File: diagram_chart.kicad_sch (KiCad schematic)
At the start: 3 parts

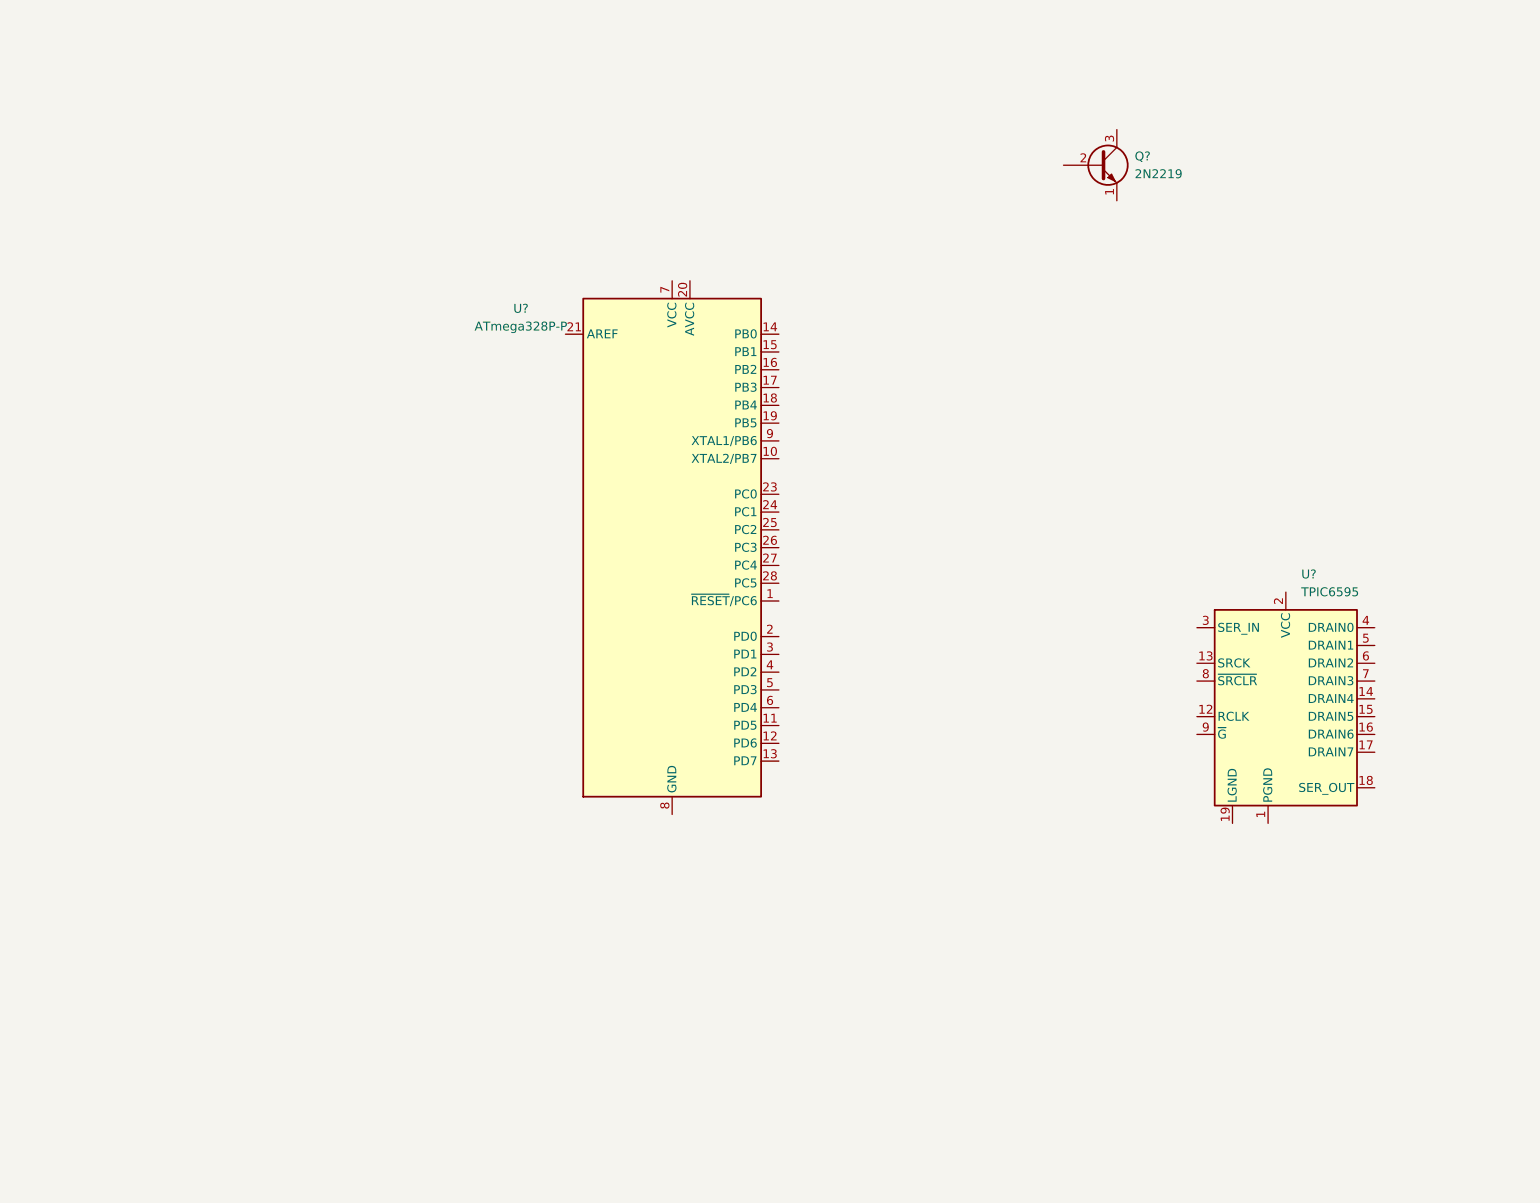
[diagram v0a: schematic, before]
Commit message: Added custom footprint and need to look at show to include it
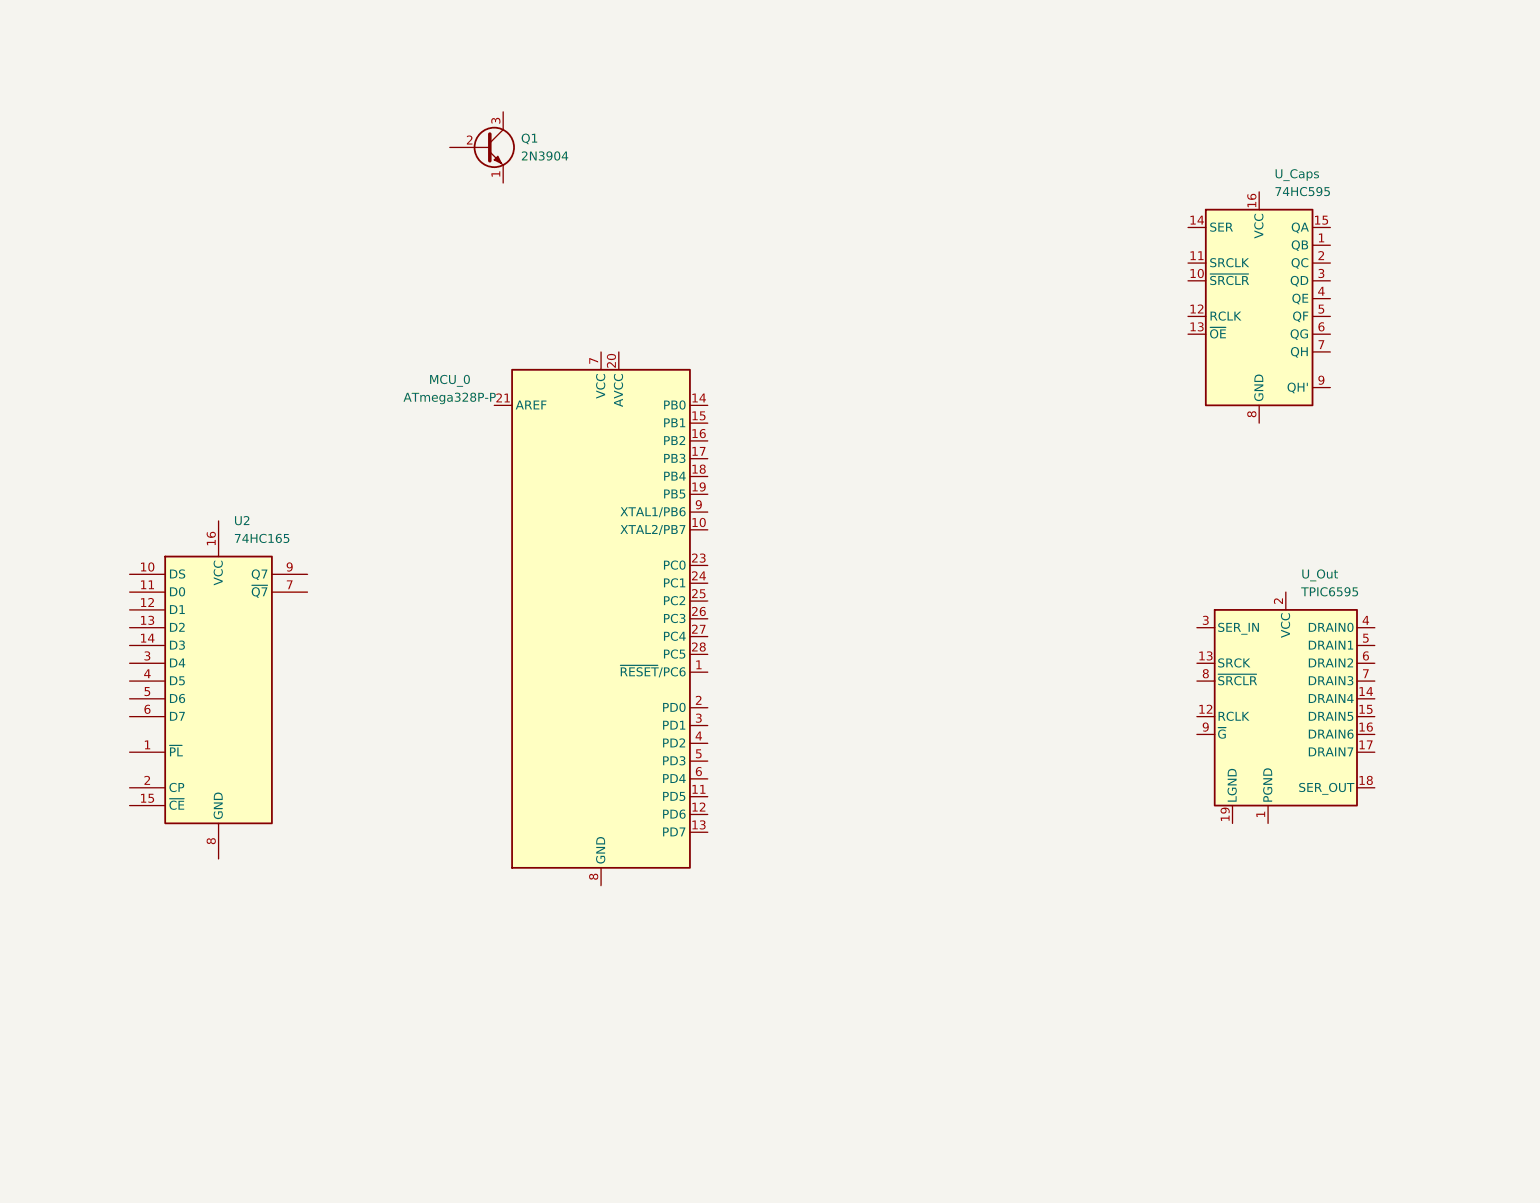
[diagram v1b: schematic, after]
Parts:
- removed Q?: 2N2219, Package_TO_SOT_THT:TO-39-3, symbol Transistor_BJT:2N2219
- added Q1: 2N3904, Package_TO_SOT_THT:TO-92_Inline, symbol Transistor_BJT:2N3904
- added U2: 74HC165, Package_DIP:DIP-16_W7.62mm_Socket, symbol 74xx:74HC165
- added U_Caps: 74HC595, Package_DIP:DIP-16_W7.62mm_Socket, symbol 74xx:74HC595
- MCU_0: renamed from U?; footprint Package_DIP:DIP-28_W7.62mm -> Package_DIP:DIP-28_W7.62mm_Socket
- U_Out: renamed from U?; footprint Package_DIP:DIP-20_W7.62mm -> Package_DIP:DIP-16_W7.62mm_Socket
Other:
- moved on the sheet: MCU_0
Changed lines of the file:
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@@
 (kicad_sch (version 20230121) (generator eeschema)
   (paper "A4")
-  (symbol (lib_id "Transistor_BJT:2N2219") (at 196.85 40.64 0) (unit 1)
+  (symbol (lib_id "74xx:74HC165") (at 71.12 114.3 0) (unit 1)
     (in_bom yes) (on_board yes) (dnp no) (fields_autoplaced)
-    (property "Reference" "Q?" (at 201.93 39.37 0)
+    (property "Reference" "U2" (at 73.3141 91.44 0)
       (effects (font (size 1.27 1.27)) (justify left))
     )
-    (property "Value" "2N2219" (at 201.93 41.91 0)
+    (property "Value" "74HC165" (at 73.3141 93.98 0)
       (effects (font (size 1.27 1.27)) (justify left))
     )
-    (property "Footprint" "Package_TO_SOT_THT:TO-39-3" (at 201.93 42.545 0)
-      (effects (font (size 1.27 1.27) italic) (justify left) hide)
+    (property "Footprint" "Package_DIP:DIP-16_W7.62mm_Socket" (at 71.12 114.3 0)
+      (effects (font (size 1.27 1.27)) hide)
     )
-    (property "Datasheet" "http://www.onsemi.com/pub_link/Collateral/2N2219-D.PDF" (at 196.85 40.64 0)
-      (effects (font (size 1.27 1.27)) (justify left) hide)
+    (property "Datasheet" "https://assets.nexperia.com/documents/data-sheet/74HC_HCT165.pdf" (at 71.12 114.3 0)
+      (effects (font (size 1.27 1.27)) hide)
     )
+    (pin "7")
+    (pin "12")
     (pin "2")
+    (pin "15")
+    (pin "13")
+    (pin "16")
+    (pin "8")
+    (pin "6")
+    (pin "9")
+    (pin "11")
+    (pin "1")
+    (pin "4")
+    (pin "10")
+    (pin "14")
     (pin "3")
-    (pin "1")
+    (pin "5")
     (instances
-      (project ""
+      (project "diagram_chart"
         (path "/6dfb841c-0ebb-4587-a5cf-7b85233b045b"
-          (reference "Q?") (unit 1)
+          (reference "U2") (unit 1)
         )
       )
     )
   )
-  (symbol (lib_id "MCU_Microchip_ATmega:ATmega328P-P") (at 135.89 95.25 0) (unit 1)
+  (symbol (lib_id "Transistor_BJT:2N3904") (at 109.22 38.1 0) (unit 1)
     (in_bom yes) (on_board yes) (dnp no) (fields_autoplaced)
-    (property "Reference" "U?" (at 114.3 61.1221 0)
+    (property "Reference" "Q1" (at 114.3 36.83 0)
+      (effects (font (size 1.27 1.27)) (justify left))
+    )
+    (property "Value" "2N3904" (at 114.3 39.37 0)
+      (effects (font (size 1.27 1.27)) (justify left))
+    )
+    (property "Footprint" "Package_TO_SOT_THT:TO-92_Inline" (at 114.3 40.005 0)
+      (effects (font (size 1.27 1.27) italic) (justify left) hide)
+    )
+    (property "Datasheet" "https://www.onsemi.com/pub/Collateral/2N3903-D.PDF" (at 109.22 38.1 0)
+      (effects (font (size 1.27 1.27)) (justify left) hide)
+    )
+    (pin "3")
+    (pin "1")
+    (pin "2")
+    (instances
+      (project "diagram_chart"
+        (path "/6dfb841c-0ebb-4587-a5cf-7b85233b045b"
+          (reference "Q1") (unit 1)
+        )
+      )
+    )
+  )
+  (symbol (lib_id "74xx:74HC595") (at 219.71 59.69 0) (unit 1)
+    (in_bom yes) (on_board yes) (dnp no) (fields_autoplaced)
+    (property "Reference" "U_Caps" (at 221.9041 41.91 0)
+      (effects (font (size 1.27 1.27)) (justify left))
+    )
+    (property "Value" "74HC595" (at 221.9041 44.45 0)
+      (effects (font (size 1.27 1.27)) (justify left))
+    )
+    (property "Footprint" "Package_DIP:DIP-16_W7.62mm_Socket" (at 219.71 59.69 0)
+      (effects (font (size 1.27 1.27)) hide)
+    )
+    (property "Datasheet" "http://www.ti.com/lit/ds/symlink/sn74hc595.pdf" (at 219.71 59.69 0)
+      (effects (font (size 1.27 1.27)) hide)
+    )
+    (pin "12")
+    (pin "4")
+    (pin "11")
+    (pin "1")
+    (pin "10")
+    (pin "5")
+    (pin "7")
+    (pin "16")
+    (pin "8")
+    (pin "6")
+    (pin "14")
+    (pin "9")
+    (pin "13")
+    (pin "3")
+    (pin "2")
+    (pin "15")
+    (instances
+      (project "diagram_chart"
+        (path "/6dfb841c-0ebb-4587-a5cf-7b85233b045b"
+          (reference "U_Caps") (unit 1)
+        )
+      )
+    )
+  )
+  (symbol (lib_id "MCU_Microchip_ATmega:ATmega328P-P") (at 125.73 105.41 0) (unit 1)
+    (in_bom yes) (on_board yes) (dnp no) (fields_autoplaced)
+    (property "Reference" "MCU_0" (at 104.14 71.2821 0)
       (effects (font (size 1.27 1.27)))
     )
-    (property "Value" "ATmega328P-P" (at 114.3 63.6621 0)
+    (property "Value" "ATmega328P-P" (at 104.14 73.8221 0)
       (effects (font (size 1.27 1.27)))
     )
-    (property "Footprint" "Package_DIP:DIP-28_W7.62mm" (at 135.89 95.25 0)
+    (property "Footprint" "Package_DIP:DIP-28_W7.62mm_Socket" (at 125.73 105.41 0)
       (effects (font (size 1.27 1.27) italic) hide)
     )
-    (property "Datasheet" "http://ww1.microchip.com/downloads/en/DeviceDoc/ATmega328_P%20AVR%20MCU%20with%20picoPower%20Technology%20Data%20Sheet%2040001984A.pdf" (at 135.89 95.25 0)
+    (property "Datasheet" "http://ww1.microchip.com/downloads/en/DeviceDoc/ATmega328_P%20AVR%20MCU%20with%20picoPower%20Technology%20Data%20Sheet%2040001984A.pdf" (at 125.73 105.41 0)
       (effects (font (size 1.27 1.27)) hide)
     )
@@
     (pin "18")
     (instances
-      (project ""
+      (project "diagram_chart"
         (path "/6dfb841c-0ebb-4587-a5cf-7b85233b045b"
-          (reference "U?") (unit 1)
+          (reference "MCU_0") (unit 1)
         )
       )
@@
   (symbol (lib_id "Interface_Expansion:TPIC6595") (at 223.52 116.84 0) (unit 1)
     (in_bom yes) (on_board yes) (dnp no) (fields_autoplaced)
-    (property "Reference" "U?" (at 225.7141 99.06 0)
+    (property "Reference" "U_Out" (at 225.7141 99.06 0)
       (effects (font (size 1.27 1.27)) (justify left))
     )
@@
       (effects (font (size 1.27 1.27)) (justify left))
     )
-    (property "Footprint" "Package_DIP:DIP-20_W7.62mm" (at 240.03 133.35 0)
+    (property "Footprint" "Package_DIP:DIP-16_W7.62mm_Socket" (at 240.03 133.35 0)
       (effects (font (size 1.27 1.27)) hide)
     )
@@
     (pin "15")
     (instances
-      (project ""
+      (project "diagram_chart"
         (path "/6dfb841c-0ebb-4587-a5cf-7b85233b045b"
-          (reference "U?") (unit 1)
+          (reference "U_Out") (unit 1)
         )
       )

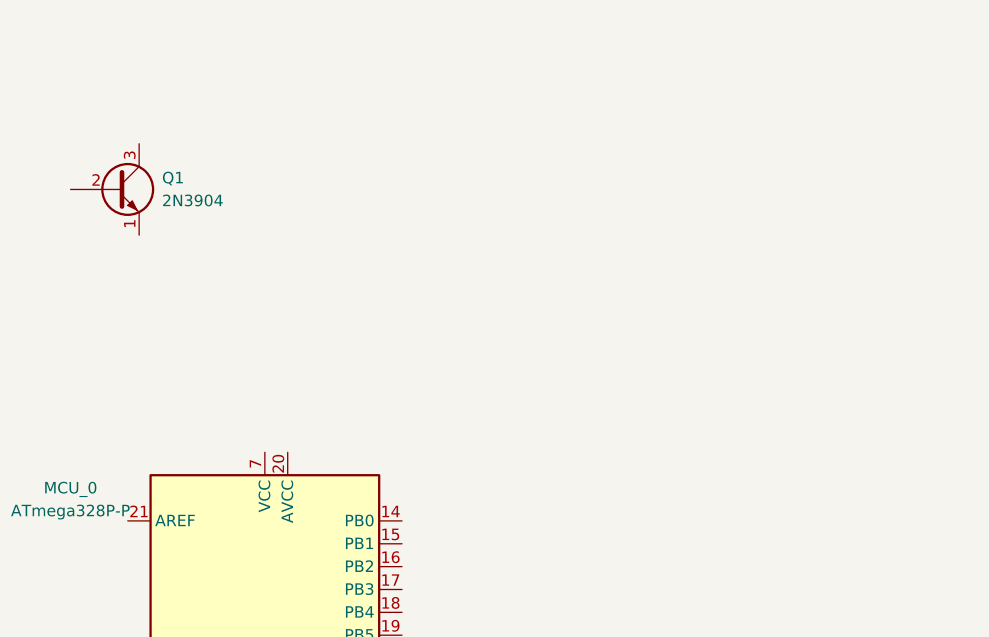
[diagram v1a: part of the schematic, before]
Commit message: Added the required Transistors, need to add DC-plug, LEDs and 7-segments
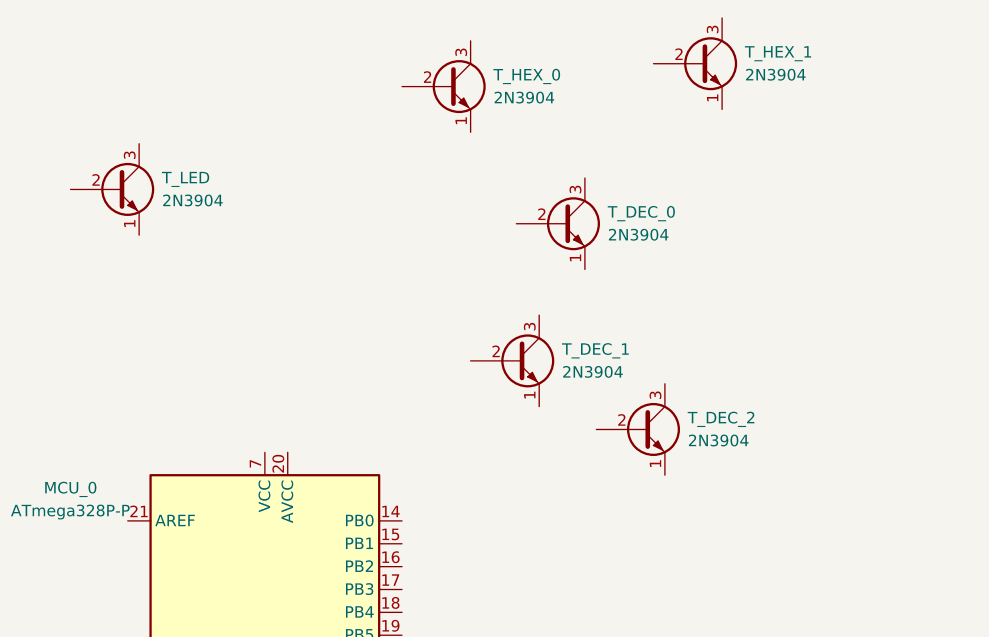
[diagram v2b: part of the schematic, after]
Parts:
- added T_DEC_0, T_DEC_1, T_DEC_2, T_HEX_0, T_HEX_1: 2N3904, Package_TO_SOT_THT:TO-92_Inline, symbol Transistor_BJT:2N3904
- renumbered Q1 to T_LED
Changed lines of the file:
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@@
+    )
+  )
+  (symbol (lib_id "Transistor_BJT:2N3904") (at 173.99 24.13 0) (unit 1)
+    (in_bom yes) (on_board yes) (dnp no) (fields_autoplaced)
+    (property "Reference" "T_HEX_1" (at 179.07 22.86 0)
+      (effects (font (size 1.27 1.27)) (justify left))
+    )
+    (property "Value" "2N3904" (at 179.07 25.4 0)
+      (effects (font (size 1.27 1.27)) (justify left))
+    )
+    (property "Footprint" "Package_TO_SOT_THT:TO-92_Inline" (at 179.07 26.035 0)
+      (effects (font (size 1.27 1.27) italic) (justify left) hide)
+    )
+    (property "Datasheet" "https://www.onsemi.com/pub/Collateral/2N3903-D.PDF" (at 173.99 24.13 0)
+      (effects (font (size 1.27 1.27)) (justify left) hide)
+    )
+    (pin "3")
+    (pin "1")
+    (pin "2")
+    (instances
+      (project "diagram_chart"
+        (path "/6dfb841c-0ebb-4587-a5cf-7b85233b045b"
+          (reference "T_HEX_1") (unit 1)
+        )
+      )
     )
   )
   (symbol (lib_id "Transistor_BJT:2N3904") (at 109.22 38.1 0) (unit 1)
     (in_bom yes) (on_board yes) (dnp no) (fields_autoplaced)
-    (property "Reference" "Q1" (at 114.3 36.83 0)
+    (property "Reference" "T_LED" (at 114.3 36.83 0)
       (effects (font (size 1.27 1.27)) (justify left))
     )
@@
       (project "diagram_chart"
         (path "/6dfb841c-0ebb-4587-a5cf-7b85233b045b"
-          (reference "Q1") (unit 1)
+          (reference "T_LED") (unit 1)
         )
       )
@@
     )
   )
+  (symbol (lib_id "Transistor_BJT:2N3904") (at 146.05 26.67 0) (unit 1)
+    (in_bom yes) (on_board yes) (dnp no) (fields_autoplaced)
+    (property "Reference" "T_HEX_0" (at 151.13 25.4 0)
+      (effects (font (size 1.27 1.27)) (justify left))
+    )
+    (property "Value" "2N3904" (at 151.13 27.94 0)
+      (effects (font (size 1.27 1.27)) (justify left))
+    )
+    (property "Footprint" "Package_TO_SOT_THT:TO-92_Inline" (at 151.13 28.575 0)
+      (effects (font (size 1.27 1.27) italic) (justify left) hide)
+    )
+    (property "Datasheet" "https://www.onsemi.com/pub/Collateral/2N3903-D.PDF" (at 146.05 26.67 0)
+      (effects (font (size 1.27 1.27)) (justify left) hide)
+    )
+    (pin "3")
+    (pin "1")
+    (pin "2")
+    (instances
+      (project "diagram_chart"
+        (path "/6dfb841c-0ebb-4587-a5cf-7b85233b045b"
+          (reference "T_HEX_0") (unit 1)
+        )
+      )
+    )
+  )
   (symbol (lib_id "Interface_Expansion:TPIC6595") (at 223.52 116.84 0) (unit 1)
     (in_bom yes) (on_board yes) (dnp no) (fields_autoplaced)
@@
         )
       )
+    )
+  )
+  (symbol (lib_id "Transistor_BJT:2N3904") (at 158.75 41.91 0) (unit 1)
+    (in_bom yes) (on_board yes) (dnp no) (fields_autoplaced)
+    (property "Reference" "T_DEC_0" (at 163.83 40.64 0)
+      (effects (font (size 1.27 1.27)) (justify left))
+    )
+    (property "Value" "2N3904" (at 163.83 43.18 0)
+      (effects (font (size 1.27 1.27)) (justify left))
+    )
+    (property "Footprint" "Package_TO_SOT_THT:TO-92_Inline" (at 163.83 43.815 0)
+      (effects (font (size 1.27 1.27) italic) (justify left) hide)
+    )
+    (property "Datasheet" "https://www.onsemi.com/pub/Collateral/2N3903-D.PDF" (at 158.75 41.91 0)
+      (effects (font (size 1.27 1.27)) (justify left) hide)
+    )
+    (pin "3")
+    (pin "1")
+    (pin "2")
+    (instances
+      (project "diagram_chart"
+        (path "/6dfb841c-0ebb-4587-a5cf-7b85233b045b"
+          (reference "T_DEC_0") (unit 1)
+        )
+      )
+    )
+  )
+  (symbol (lib_id "Transistor_BJT:2N3904") (at 167.64 64.77 0) (unit 1)
+    (in_bom yes) (on_board yes) (dnp no) (fields_autoplaced)
+    (property "Reference" "T_DEC_2" (at 172.72 63.5 0)
+      (effects (font (size 1.27 1.27)) (justify left))
+    )
+    (property "Value" "2N3904" (at 172.72 66.04 0)
+      (effects (font (size 1.27 1.27)) (justify left))
+    )
+    (property "Footprint" "Package_TO_SOT_THT:TO-92_Inline" (at 172.72 66.675 0)
+      (effects (font (size 1.27 1.27) italic) (justify left) hide)
+    )
+    (property "Datasheet" "https://www.onsemi.com/pub/Collateral/2N3903-D.PDF" (at 167.64 64.77 0)
+      (effects (font (size 1.27 1.27)) (justify left) hide)
+    )
+    (pin "3")
+    (pin "1")
+    (pin "2")
+    (instances
+      (project "diagram_chart"
+        (path "/6dfb841c-0ebb-4587-a5cf-7b85233b045b"
+          (reference "T_DEC_2") (unit 1)
+        )
+      )
+    )
+  )
+  (symbol (lib_id "Transistor_BJT:2N3904") (at 153.67 57.15 0) (unit 1)
+    (in_bom yes) (on_board yes) (dnp no) (fields_autoplaced)
+    (property "Reference" "T_DEC_1" (at 158.75 55.88 0)
+      (effects (font (size 1.27 1.27)) (justify left))
+    )
+    (property "Value" "2N3904" (at 158.75 58.42 0)
+      (effects (font (size 1.27 1.27)) (justify left))
+    )
+    (property "Footprint" "Package_TO_SOT_THT:TO-92_Inline" (at 158.75 59.055 0)
+      (effects (font (size 1.27 1.27) italic) (justify left) hide)
+    )
+    (property "Datasheet" "https://www.onsemi.com/pub/Collateral/2N3903-D.PDF" (at 153.67 57.15 0)
+      (effects (font (size 1.27 1.27)) (justify left) hide)
+    )
+    (pin "3")
+    (pin "1")
+    (pin "2")
+    (instances
+      (project "diagram_chart"
+        (path "/6dfb841c-0ebb-4587-a5cf-7b85233b045b"
+          (reference "T_DEC_1") (unit 1)
+        )
+      )
